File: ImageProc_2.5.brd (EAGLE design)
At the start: 49.8 x 23.2 mm, 115 parts, among them IC1 XC61GC3002HR-G, IC10 AT45DB642D-CNU, IC2 MIC5335-SPYMT, IC3 MIC5335-JGYMT, IC4 DSPIC33FJ128MC706A, IC5 AT86RF233-ZU, IC6 LTC6088, IC7 DRV8833RTY, IC8 DRV8833RTY, IC9 MPU-6000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

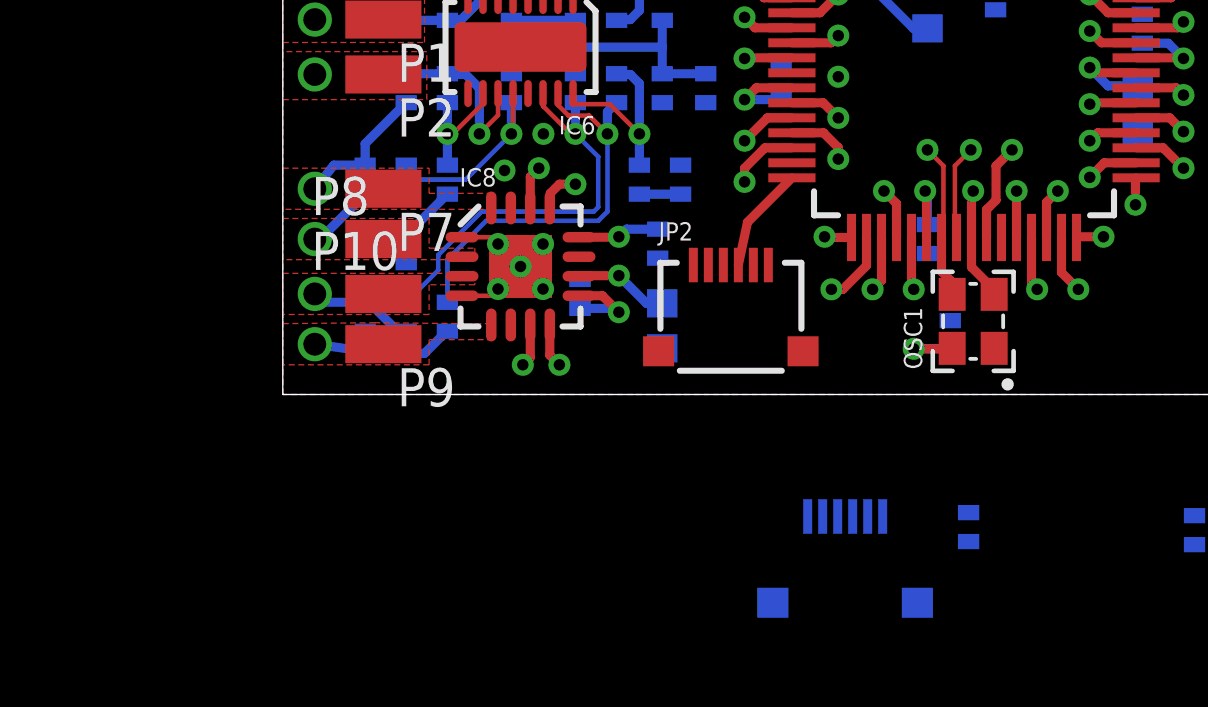
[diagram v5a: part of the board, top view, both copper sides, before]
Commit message: Added anti-aliasing filter values (not sure how I missed those). Renamed external pins.
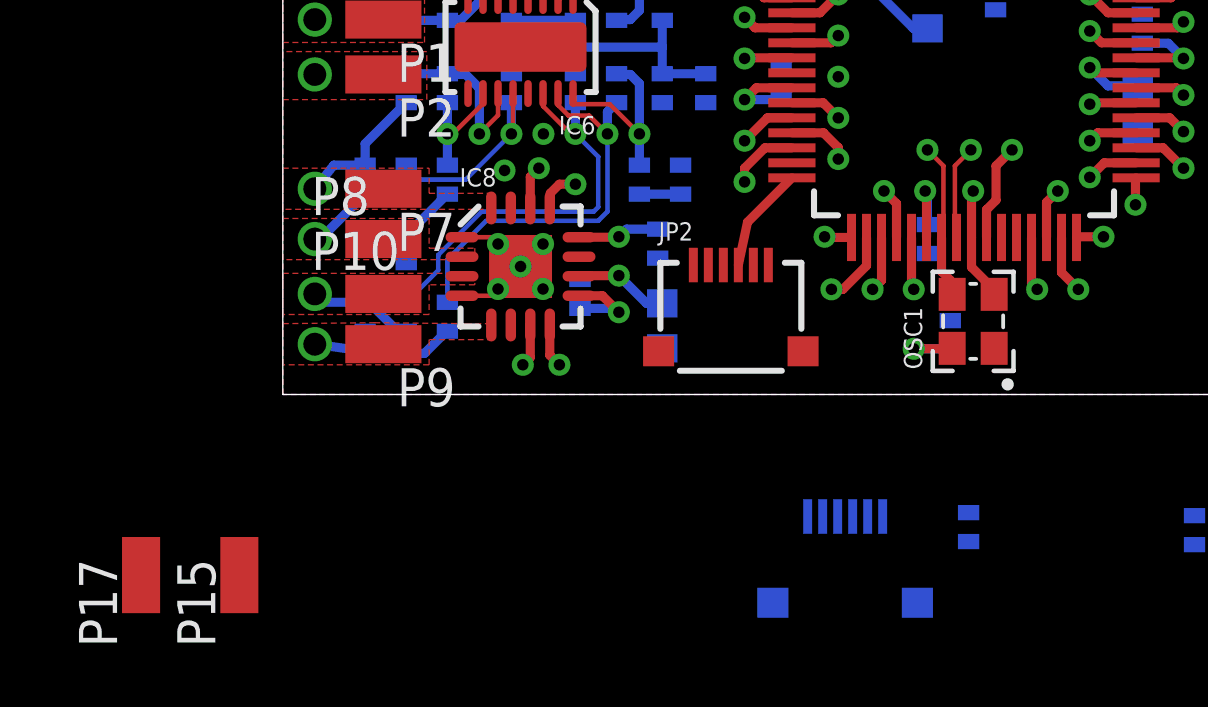
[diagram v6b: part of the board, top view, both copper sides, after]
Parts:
- added P15, P17: EXT5, wirepad:SMD1,27-2,54
- C41, C42, C44: value (none) -> 2.2nF
- C43: value xnF -> 2.2nF
- P16: value EXT6 -> EXT5
- R29, R30, R31, R32: value (none) -> 1k
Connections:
- net EXT1 renamed AN1/RB1
- net EXT2 renamed AN3/INDX/RB3
- net EXT3 renamed AN4/QEA/IC7/RB4
- net EXT4 renamed AN5/QEB/IC8/RB5
- net EXT6 renamed IC3/INT3/RD10
- net 3.3V: now also P17.1
- net GND: now also P15.1
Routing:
- net IC3/INT3/RD10: track 1.55 -> 0.00 mm, vias 1 -> 0

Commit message: first few routes on ground
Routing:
- net CAM_PWDN: track 4.10 -> 36.7 mm
- net MOTOR_C_IN1: track 2.36 -> 31.0 mm
- net MOTOR_C_IN2: track 2.41 -> 25.2 mm
- net MOTOR_C_BEMF: track 3.56 -> 17.0 mm
- net MOTOR_B_BEMF: track 3.64 -> 12.8 mm
- net 2.5V: track 12.8 -> 5.14 mm

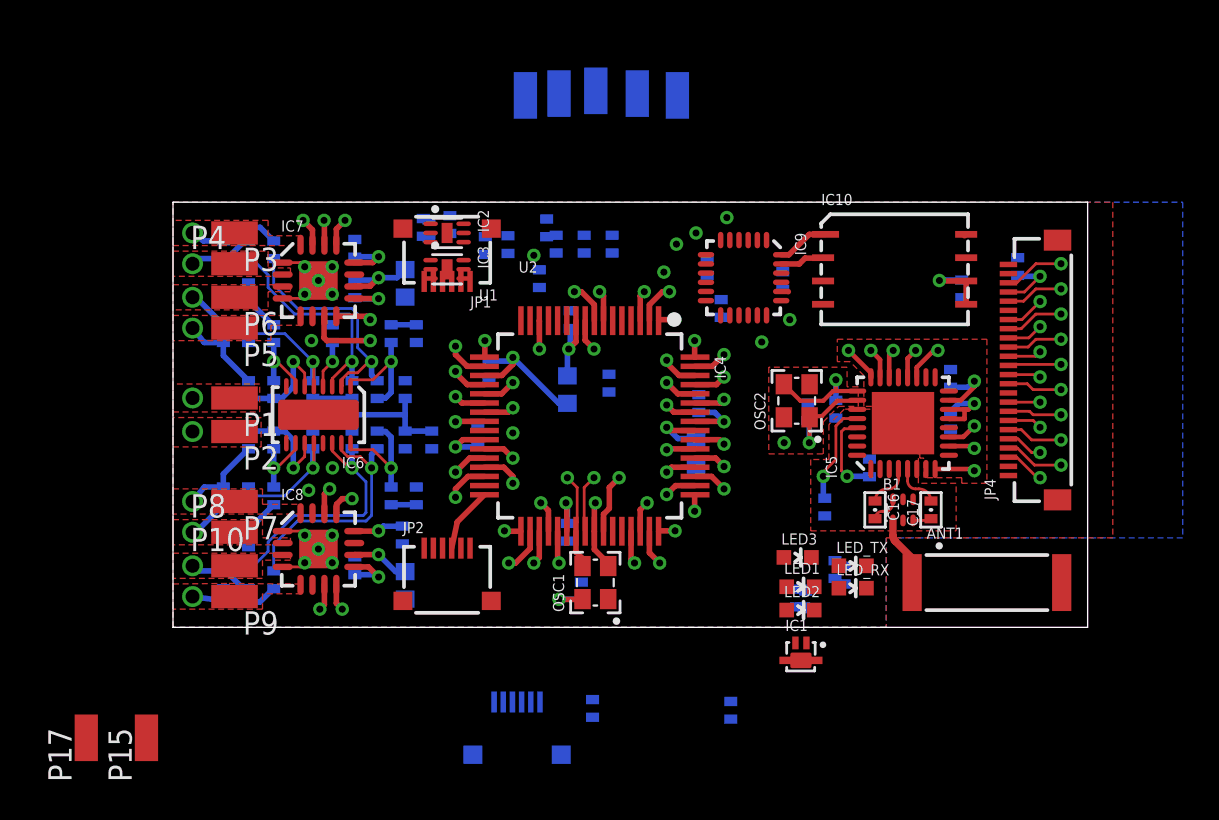
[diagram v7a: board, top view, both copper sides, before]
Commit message: Routed Several more connections.
Placed LEDS and added vias for it.

Placed Connector On Bottom.

Deleted some badly planned connections from last time.
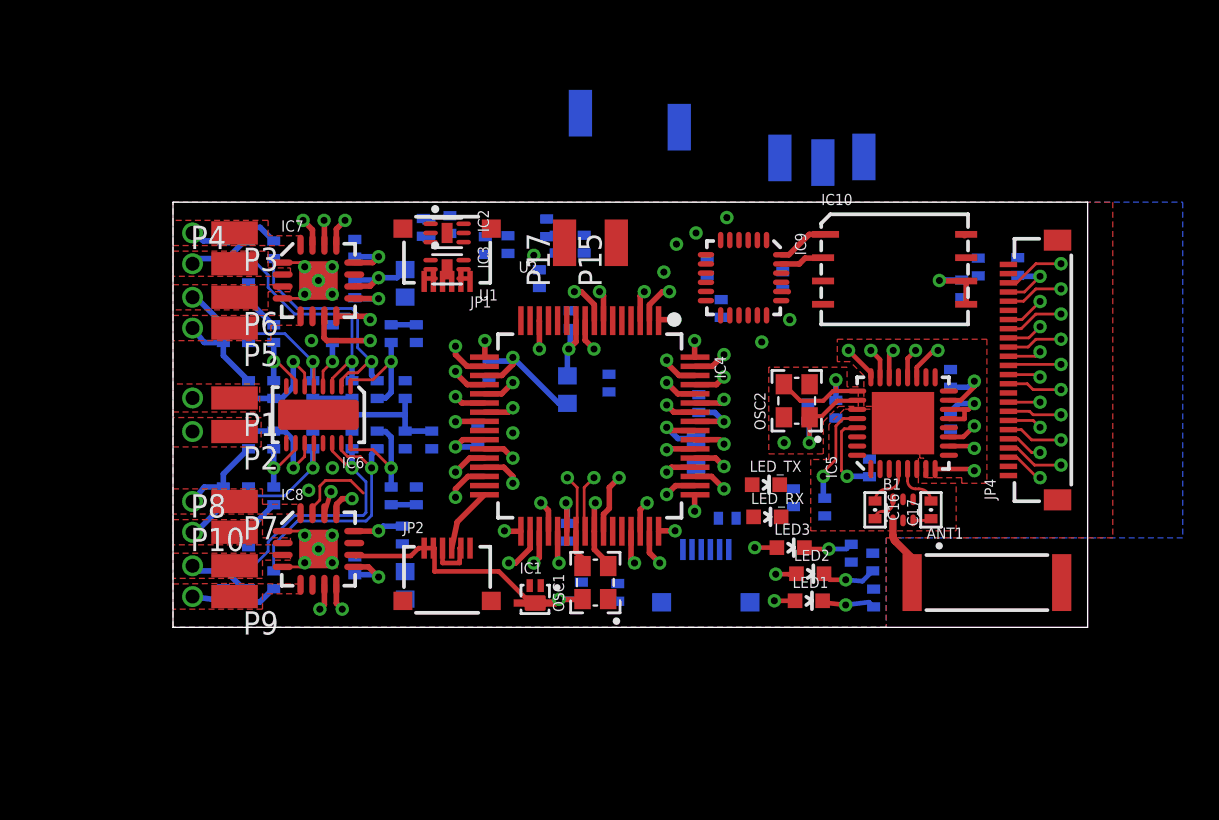
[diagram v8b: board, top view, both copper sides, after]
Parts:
- moved P17 37.5 mm to (21.3, 21.0)
- moved P15 37.2 mm to (24.2, 21.0)
- moved R5 27.7 mm to (43.9, 19.6)
- moved P16 18.7 mm to (37.6, 25.6)
- moved IC1 14.8 mm to (19.7, 1.52)
- moved JP3 13.2 mm to (29.0, 2.51)
- moved P14 8.73 mm to (35.4, 25.3)
- moved P12 8.53 mm to (33.1, 25.6)
- moved R7 7.09 mm to (30.2, 5.94), turned to 180 degrees
- moved P11 6.80 mm to (27.6, 27.3)
- moved R4 6.47 mm to (24.2, 1.91)
- moved LED_TX 6.47 mm to (32.3, 7.77)
- moved LED_RX 6.06 mm to (32.4, 6.02)
- moved R6 4.52 mm to (33.8, 7.06), turned to 270 degrees
- moved R27 4.20 mm to (38.1, 3.56)
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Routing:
- net SDA1: track 5.06 -> 35.8 mm
- net MOTOR_C_IN1: track 31.0 -> 2.15 mm
- net GN_LED: track 1.89 -> 30.1 mm, vias 1 -> 2
- net MOTOR_C_IN2: track 25.2 -> 2.41 mm
- net YW_LED: track 2.13 -> 22.6 mm, vias 1 -> 2
- net RD_LED: track 1.75 -> 21.9 mm, vias 1 -> 2
- net V_BATT: track 9.41 -> 22.7 mm, vias 4 -> 3
- net CAM_HREF: track 26.9 -> 34.6 mm
- net N$15: track 0.00 -> 3.23 mm, vias 0 -> 1
- net N$16: track 0.00 -> 3.03 mm, vias 0 -> 1
- net N$17: track 0.00 -> 2.69 mm, vias 0 -> 1
- net GND: track 12.7 -> 15.4 mm
